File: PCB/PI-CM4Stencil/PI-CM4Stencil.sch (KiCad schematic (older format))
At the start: 1 part, among them U1 Pi_CM4

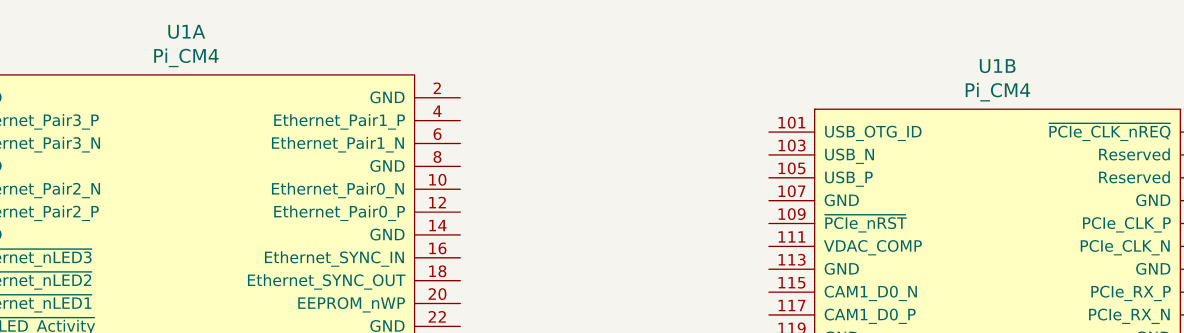
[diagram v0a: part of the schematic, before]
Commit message: Revert "Created gerber files"
This reverts commit b53c7857d78f5a39796a9ae11ef4b5de09c35e59.
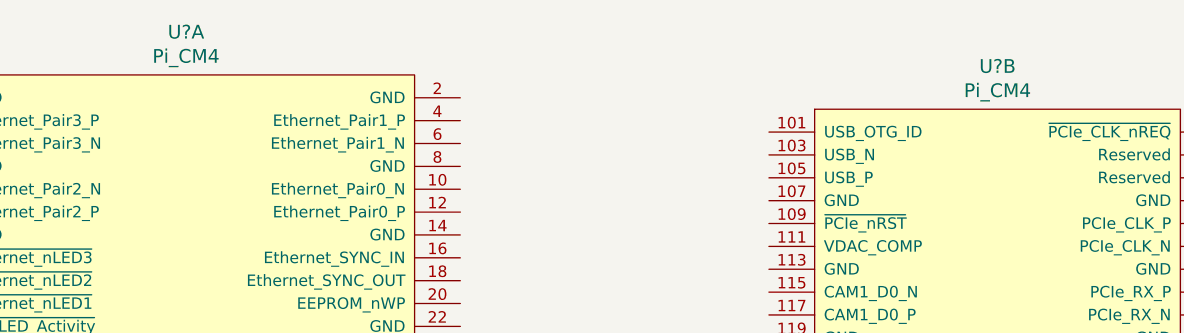
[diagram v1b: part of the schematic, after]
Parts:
- U? (x2): renamed from U1; footprint PI-CM4Stencil:Pi_CM4 -> (none)
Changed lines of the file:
@@
 $EndDescr
 $Comp
-L PI-CM4Stencil:Pi_CM4 U1
+L PI-CM4Stencil:Pi_CM4 U?
 U 1 1 61E11F1A
 P 2650 1150
-F 0 "U1" H 3850 1437 60  0000 C CNN
+F 0 "U?" H 3850 1437 60  0000 C CNN
 F 1 "Pi_CM4" H 3850 1331 60  0000 C CNN
-F 2 "PI-CM4Stencil:Pi_CM4" H 2850 1200 60  0001 L CNN
+F 2 "" H 2850 1200 60  0001 L CNN
 F 3 "" H 2850 1000 60  0001 L CNN
 	1    2650 1150
@@
 $EndComp
 $Comp
-L PI-CM4Stencil:Pi_CM4 U1
+L PI-CM4Stencil:Pi_CM4 U?
 U 2 1 61E1AEBE
 P 6400 1300
-F 0 "U1" H 7400 1587 60  0000 C CNN
+F 0 "U?" H 7400 1587 60  0000 C CNN
 F 1 "Pi_CM4" H 7400 1481 60  0000 C CNN
-F 2 "PI-CM4Stencil:Pi_CM4" H 6600 1350 60  0001 L CNN
+F 2 "" H 6600 1350 60  0001 L CNN
 F 3 "" H 6600 1150 60  0001 L CNN
 	2    6400 1300

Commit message: Created gerber files
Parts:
- U1: renamed from U?; footprint (none) -> PI-CM4Stencil:Pi_CM4
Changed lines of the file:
@@
 $EndDescr
 $Comp
-L PI-CM4Stencil:Pi_CM4 U?
+L PI-CM4Stencil:Pi_CM4 U1
 U 1 1 61E11F1A
 P 2650 1150
-F 0 "U?" H 3850 1437 60  0000 C CNN
+F 0 "U1" H 3850 1437 60  0000 C CNN
 F 1 "Pi_CM4" H 3850 1331 60  0000 C CNN
-F 2 "" H 2850 1200 60  0001 L CNN
+F 2 "PI-CM4Stencil:Pi_CM4" H 2850 1200 60  0001 L CNN
 F 3 "" H 2850 1000 60  0001 L CNN
 	1    2650 1150
@@
 $EndComp
 $Comp
-L PI-CM4Stencil:Pi_CM4 U?
+L PI-CM4Stencil:Pi_CM4 U1
 U 2 1 61E1AEBE
 P 6400 1300
-F 0 "U?" H 7400 1587 60  0000 C CNN
+F 0 "U1" H 7400 1587 60  0000 C CNN
 F 1 "Pi_CM4" H 7400 1481 60  0000 C CNN
-F 2 "" H 6600 1350 60  0001 L CNN
+F 2 "PI-CM4Stencil:Pi_CM4" H 6600 1350 60  0001 L CNN
 F 3 "" H 6600 1150 60  0001 L CNN
 	2    6400 1300
